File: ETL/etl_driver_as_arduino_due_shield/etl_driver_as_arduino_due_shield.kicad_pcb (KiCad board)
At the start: 2 copper layers, 69.6 x 33.5 mm, 15 parts, among them J1 Analog in, J2 12V power, J3 to_ETL, Q1 BD441, U1 CA3140

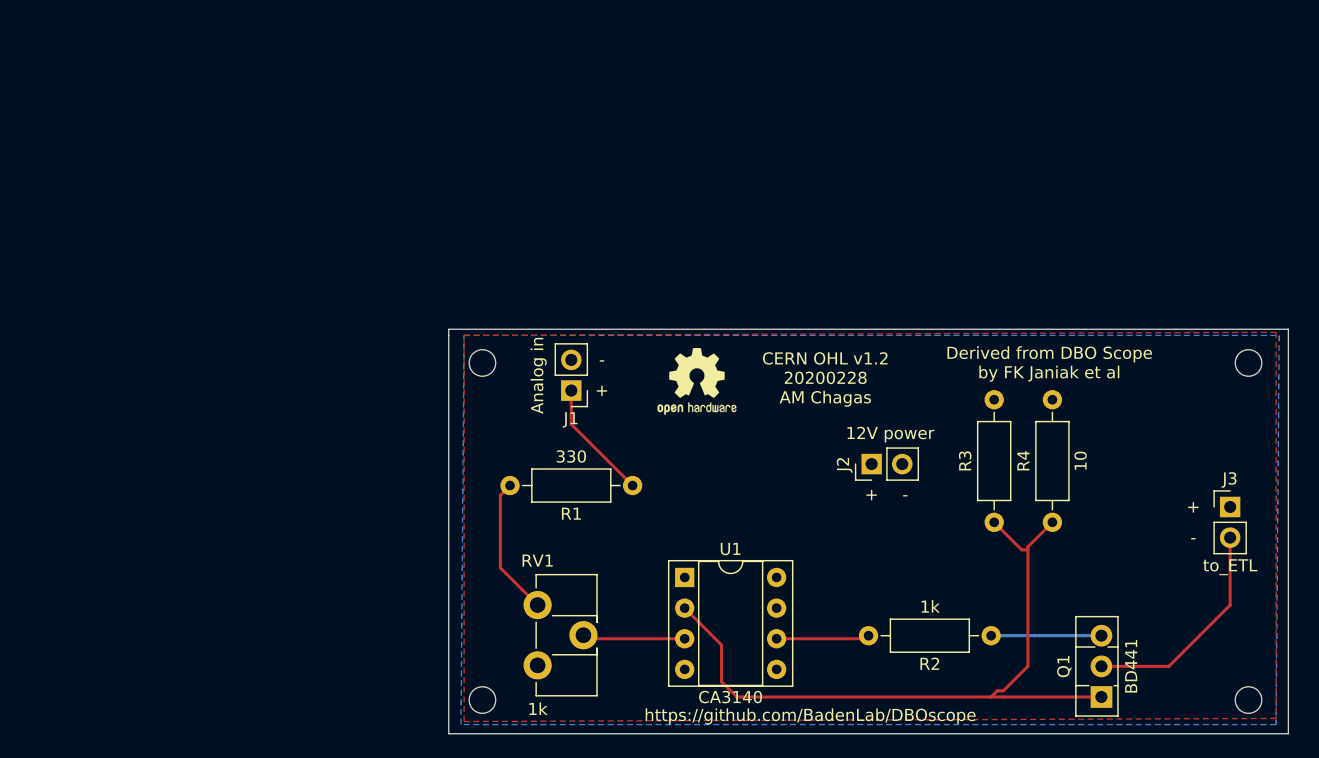
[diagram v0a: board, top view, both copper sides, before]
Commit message: add arduino due shield for lens driver
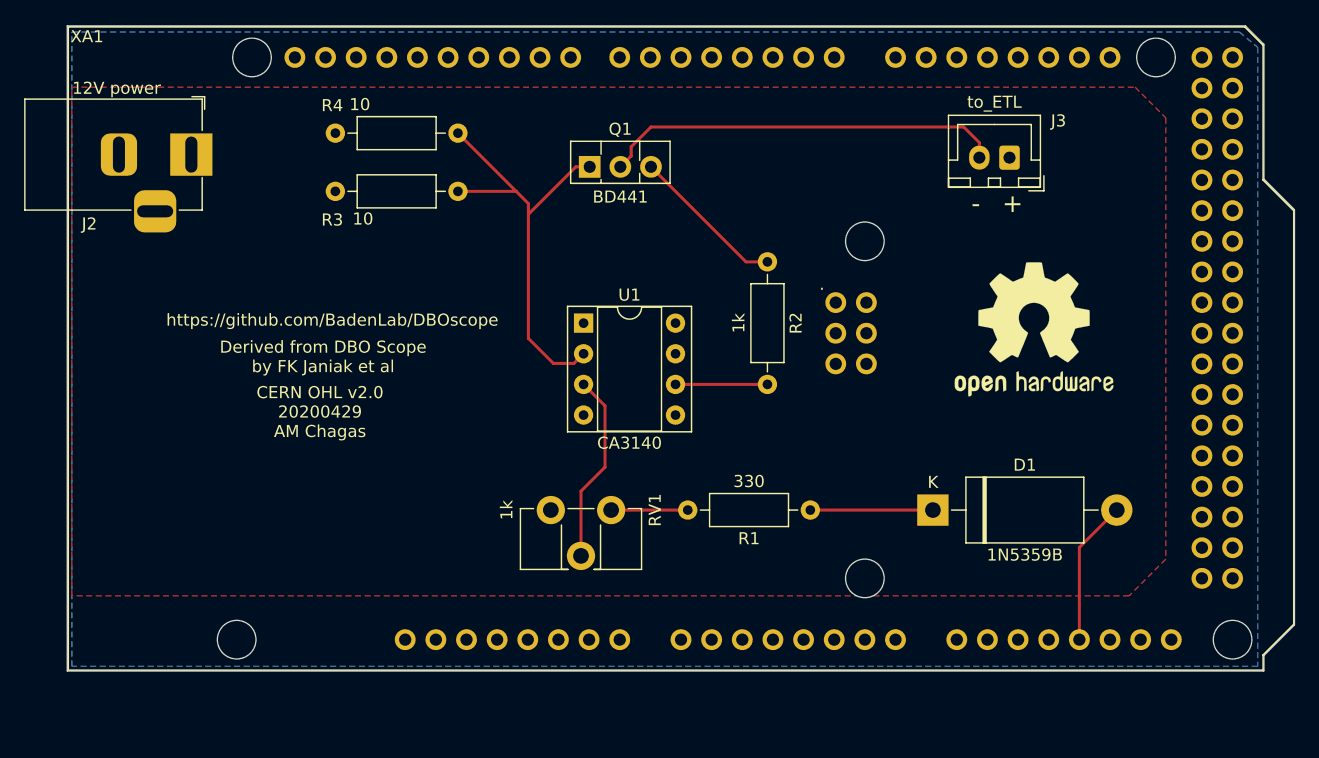
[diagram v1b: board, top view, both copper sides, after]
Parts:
- removed J1: Analog in, Connector_PinHeader_2.54mm:PinHeader_1x02_P2.54mm_Vertical
- removed the REF** at (126.7, 127.3)
- removed the REF** at (126.7, 99.3)
- removed the REF** at (190.2, 99.3)
- removed the REF** at (190.2, 127.3)
- removed the REF** at (144.5, 100.8)
- added D1: 1N5359B, Diode_THT:D_DO-201_P15.24mm_Horizontal, F.Cu at (164.1, 111.5)
- added REF**: OSHW-Logo2_14.6x12mm_SilkScreen, Symbol:OSHW-Logo2_14.6x12mm_SilkScreen, F.Cu at (172.5, 96.5)
- added XA1: Arduino_Due_Shield, Arduino:Arduino_Due_Shield, F.Cu at (92.4, 124.8)
- J2: footprint Connector_PinHeader_2.54mm:PinHeader_1x02_P2.54mm_Vertical -> Connector_BarrelJack:BarrelJack_Horizontal
- J3: footprint Connector_PinHeader_2.54mm:PinHeader_1x02_P2.54mm_Vertical -> Connector_JST:JST_XH_B2B-XH-A_1x02_P2.50mm_Vertical
- moved J2 61.9 mm to (102.6, 82.0), turned to 0 degrees
- moved Q1 61.1 mm to (135.6, 83.1), turned to 0 degrees
- moved R4 58.9 mm to (124.7, 80.3), turned to 180 degrees
- moved R3 52.2 mm to (124.7, 85.1), turned to 180 degrees
- moved R2 36.1 mm to (150.4, 90.9), turned to 270 degrees
- moved J3 34.2 mm to (170.4, 82.3), turned to 180 degrees
- moved U1 22.7 mm to (135.1, 96.0)
- moved R1 14.9 mm to (153.9, 111.5)
- moved RV1 9.96 mm to (137.4, 111.5), turned to 270 degrees
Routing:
- net Net-(Q1-Pad1): track 60.3 -> 36.7 mm
- net Net-(J3-Pad2): track 18.4 -> 33.4 mm
- net Net-(D1-Pad2): track 0.00 -> 12.0 mm
- net Net-(RV1-Pad2): track 8.51 -> 15.8 mm
- net Net-(R1-Pad2): track 11.5 -> 6.35 mm
- net Net-(Q1-Pad3): track 9.14 -> 12.9 mm
- added copper zone on F.Cu, net +12V
- added copper zone on B.Cu, net GND
- removed copper zone on B.Cu, net +12V
- removed copper zone on F.Cu, net GND
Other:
- board size 69.6 x 33.5 mm -> 101.7 x 53.5 mm
- board text added: "CERN OHL v2.0 20200429 AM Chagas"
- board text removed: "CERN OHL v1.2 20200228 AM Chagas"
